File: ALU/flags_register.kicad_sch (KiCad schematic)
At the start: 7 parts, among them U6 SN74F86N, U8 Dual D FF

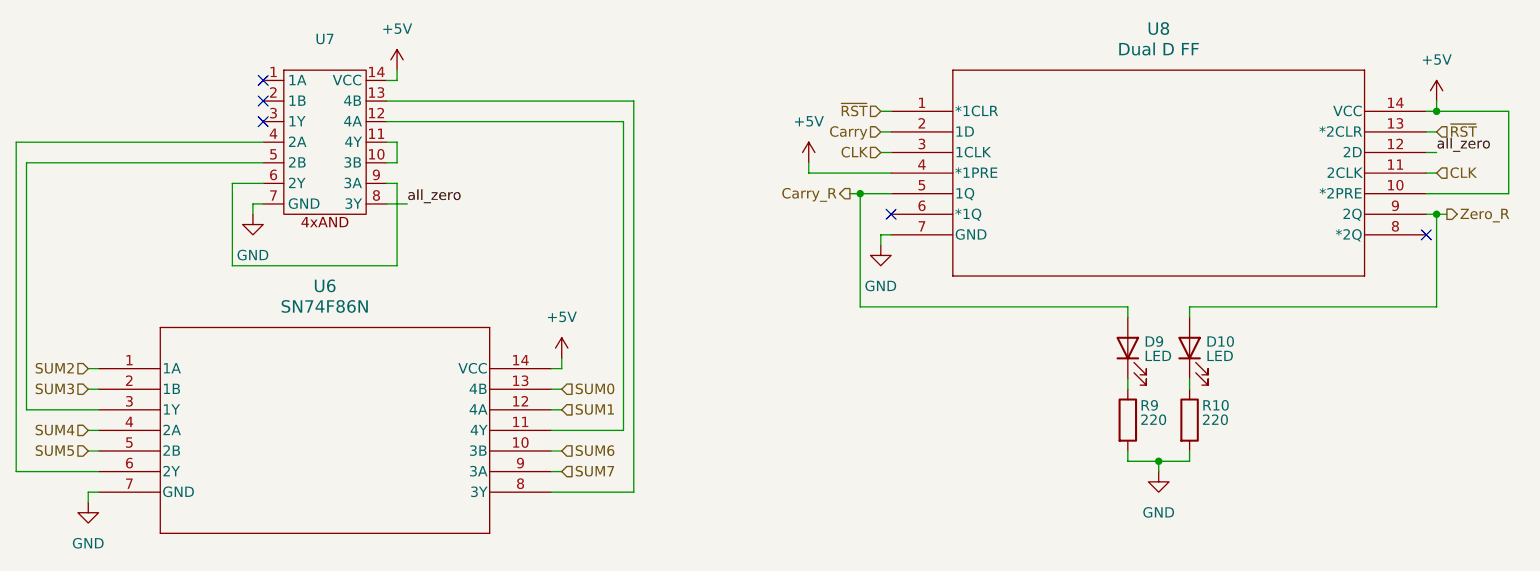
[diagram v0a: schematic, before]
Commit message: 4x NOR pinout was wrong. Updated with correct pinout. Fixed 2x D flip-flop references
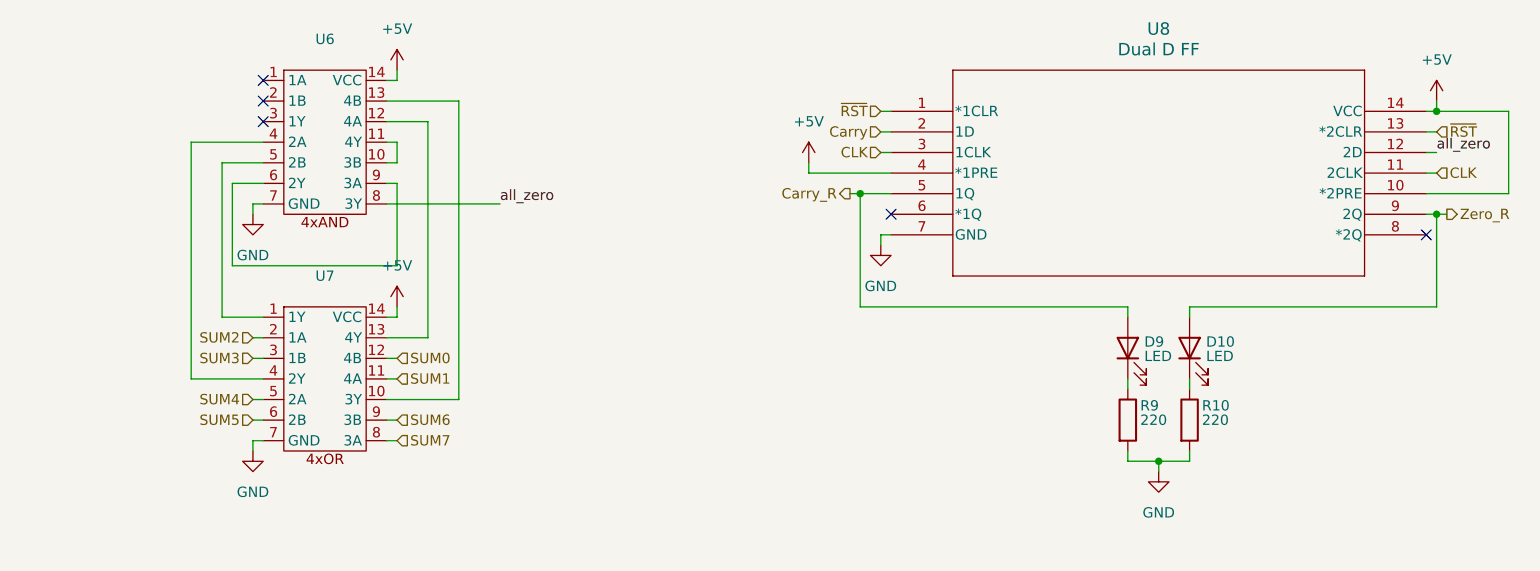
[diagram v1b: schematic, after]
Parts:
- removed U6: SN74F86N, _DownloadFootprints:4x_nor, symbol 4x_xor:SN74F86N
- added U7: ~, Package_DIP:DIP-14_W7.62mm, symbol 8BitCPU:4x_or
- U8: symbol 4x_D_FF:SN74HC74N -> 2x_D_FF:SN74HC74N
- renumbered U7 to U6
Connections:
- net +5V: now also U7.14 (VCC)
- net GND: now also U7.7 (GND)
- net SUM0: now also U7.12 (4B)
- net SUM1: now also U7.11 (4A)
- net SUM2: now also U7.2 (1A)
- net SUM3: now also U7.3 (1B)
- net SUM4: now also U7.5 (2A)
- net SUM5: now also U7.6 (2B)
- net SUM6: now also U7.9 (3B)
- net SUM7: now also U7.8 (3A)
- net at U6.12 (4A): now also U7.13 (4Y)
- net at U6.5 (2B): now also U7.1 (1Y)
- net at U6.4 (2A): now also U7.4 (2Y)
- net at U6.13 (4B): now also U7.10 (3Y)

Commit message: Fixed NOR schematic labeled as OR in ALU
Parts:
- removed U7: ~, Package_DIP:DIP-14_W7.62mm, symbol 8BitCPU:4x_or
- added U7: ~, Package_DIP:DIP-14_W7.62mm, symbol 8BitCPU:4x_nor
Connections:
- net +5V: now also U7.14 (VCC)
- net GND: now also U7.7 (GND)
- net SUM0: now also U7.12 (4B)
- net SUM1: now also U7.11 (4A)
- net SUM2: now also U7.2 (1A)
- net SUM3: now also U7.3 (1B)
- net SUM4: now also U7.5 (2A)
- net SUM5: now also U7.6 (2B)
- net SUM6: now also U7.9 (3B)
- net SUM7: now also U7.8 (3A)
- net at U6.5 (2B): now also U7.1 (1Y)
- net at U6.13 (4B): now also U7.10 (3Y)
- net at U6.12 (4A): now also U7.13 (4Y)
- net at U6.4 (2A): now also U7.4 (2Y)
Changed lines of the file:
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@@
-	)
-	(symbol
-		(lib_id "8BitCPU:4x_or")
-		(at 99.06 107.95 0)
-		(unit 1)
-		(exclude_from_sim no)
-		(in_bom yes)
-		(on_board yes)
-		(dnp no)
-		(fields_autoplaced yes)
-		(property "Reference" "U7"
-			(at 99.06 96.52 0)
-			(effects
-				(font
-					(size 1.27 1.27)
-				)
-			)
-		)
-		(property "Value" "~"
-			(at 99.06 99.06 0)
-			(effects
-				(font
-					(size 1.27 1.27)
-				)
-			)
-		)
-		(property "Footprint" "Package_DIP:DIP-14_W7.62mm"
-			(at 99.06 107.95 0)
-			(effects
-				(font
-					(size 1.27 1.27)
-				)
-				(hide yes)
-			)
-		)
-		(property "Datasheet" ""
-			(at 99.06 107.95 0)
-			(effects
-				(font
-					(size 1.27 1.27)
-				)
-				(hide yes)
-			)
-		)
-		(property "Description" ""
-			(at 99.06 107.95 0)
-			(effects
-				(font
-					(size 1.27 1.27)
-				)
-				(hide yes)
-			)
-		)
-		(pin "5"
-		)
-		(pin "7"
-		)
-		(pin "12"
-		)
-		(pin "13"
-		)
-		(pin "9"
-		)
-		(pin "4"
-		)
-		(pin "6"
-		)
-		(pin "10"
-		)
-		(pin "14"
-		)
-		(pin "2"
-		)
-		(pin "3"
-		)
-		(pin "8"
-		)
-		(pin "11"
-		)
-		(pin "1"
-		)
-		(instances
-			(project ""
-				(path "/62101b97-a334-4edf-8cb6-c85e816b5b90/6c41eb69-b663-40ea-b582-19e471384745"
-					(reference "U7")
-					(unit 1)
-				)
-			)
-		)
 	)
 	(symbol
@@
 					(unit 1)
 				)
+			)
+		)
+	)
+	(symbol
+		(lib_id "8BitCPU:4x_nor")
+		(at 99.06 107.95 0)
+		(unit 1)
+		(exclude_from_sim no)
+		(in_bom yes)
+		(on_board yes)
+		(dnp no)
+		(fields_autoplaced yes)
+		(property "Reference" "U7"
+			(at 99.06 96.52 0)
+			(effects
+				(font
+					(size 1.27 1.27)
+				)
+			)
+		)
+		(property "Value" "~"
+			(at 99.06 99.06 0)
+			(effects
+				(font
+					(size 1.27 1.27)
+				)
+			)
+		)
+		(property "Footprint" "Package_DIP:DIP-14_W7.62mm"
+			(at 99.06 107.95 0)
+			(effects
+				(font
+					(size 1.27 1.27)
+				)
+				(hide yes)
+			)
+		)
+		(property "Datasheet" ""
+			(at 99.06 107.95 0)
+			(effects
+				(font
+					(size 1.27 1.27)
+				)
+				(hide yes)
+			)
+		)
+		(property "Description" ""
+			(at 99.06 107.95 0)
+			(effects
+				(font
+					(size 1.27 1.27)
+				)
+				(hide yes)
+			)
+		)
+		(pin "6"
+		)
+		(pin "1"
+		)
+		(pin "13"
+		)
+		(pin "11"
+		)
+		(pin "2"
+		)
+		(pin "3"
+		)
+		(pin "8"
+		)
+		(pin "7"
+		)
+		(pin "5"
+		)
+		(pin "14"
+		)
+		(pin "12"
+		)
+		(pin "9"
+		)
+		(pin "10"
+		)
+		(pin "4"
+		)
+		(instances
+			(project ""
+				(path "/62101b97-a334-4edf-8cb6-c85e816b5b90/6c41eb69-b663-40ea-b582-19e471384745"
+					(reference "U7")
+					(unit 1)
+				)

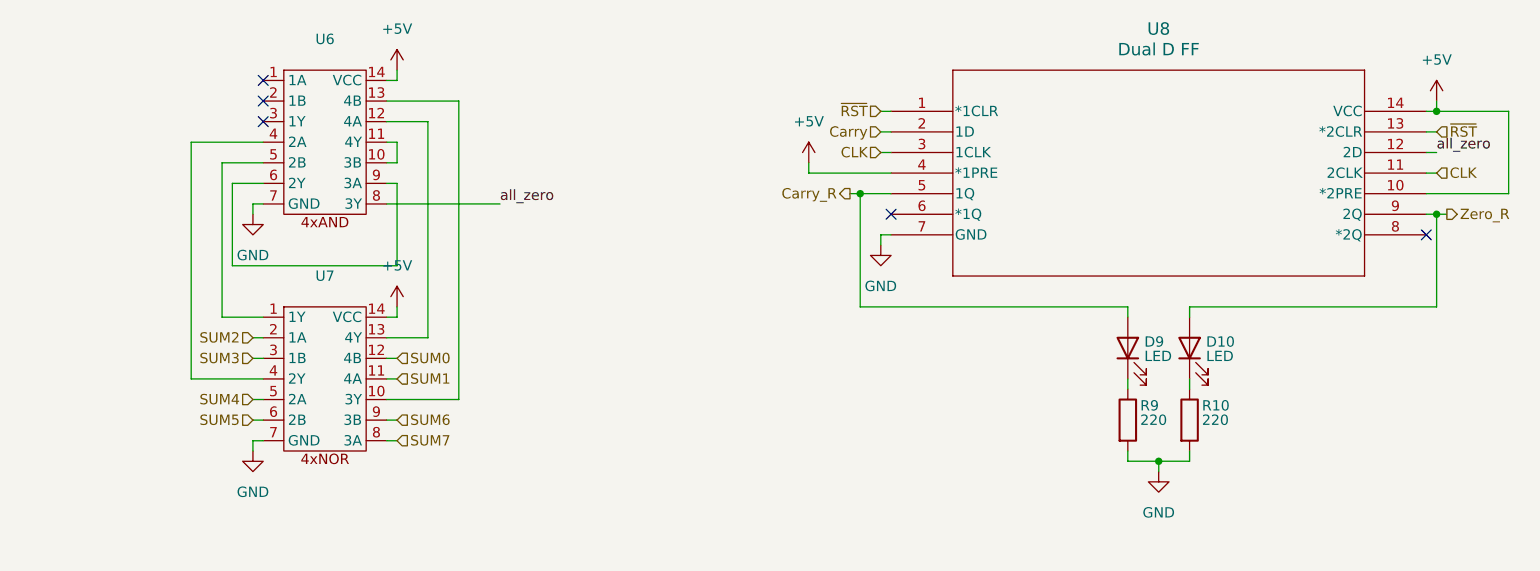
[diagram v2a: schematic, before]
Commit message: Forgot Flags register input enable. Passing clock though spare AND gate with new input Flag In input to create equvilant
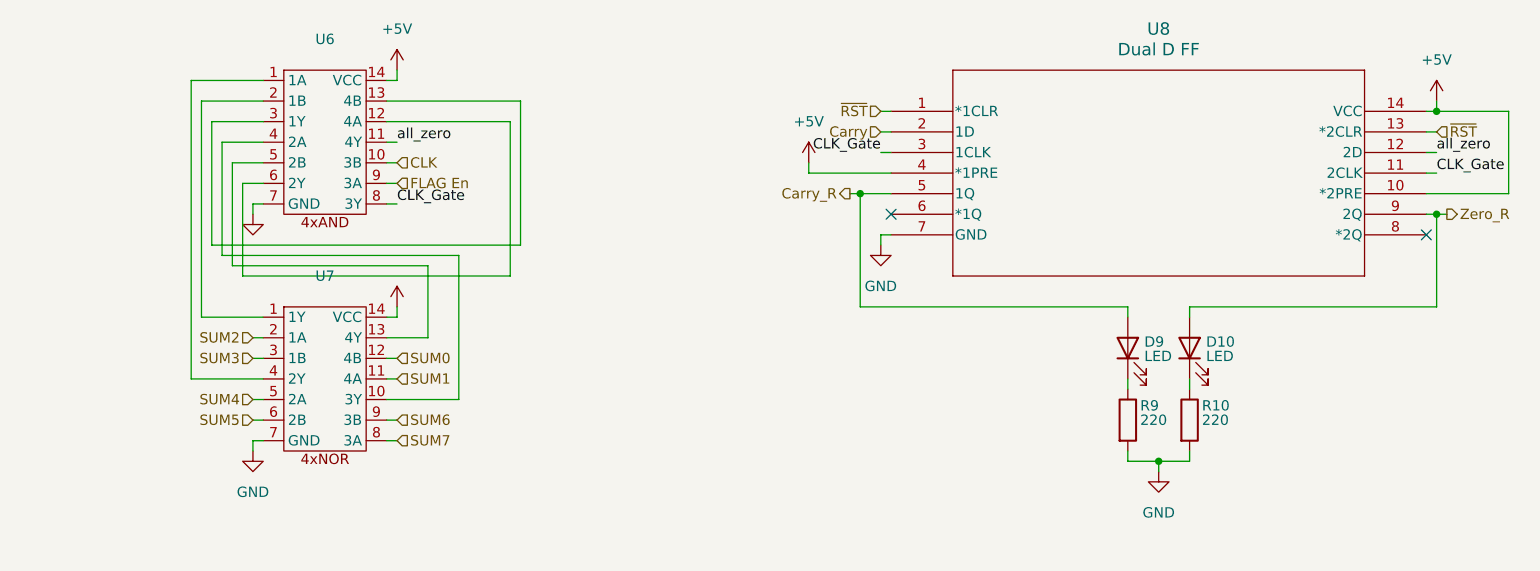
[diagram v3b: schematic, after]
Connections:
- net CLK: now also U6.10 (3B); no longer U8.11 (2CLK), U8.3 (1CLK)
- net all_zero: now also U6.11 (4Y); no longer U6.8 (3Y)
- net at U7.1 (1Y): now also U6.2 (1B); no longer U6.5 (2B)
- net at U7.10 (3Y): now also U6.4 (2A); no longer U6.13 (4B)
- net at U7.13 (4Y): now also U6.5 (2B); no longer U6.12 (4A)
- net at U7.4 (2Y): now also U6.1 (1A); no longer U6.4 (2A)
- net at U6.3 (1Y): now also U6.13 (4B)
- net at U6.6 (2Y): now also U6.12 (4A); no longer U6.9 (3A)
- new net CLK_Gate: U6.8 (3Y), U8.11 (2CLK), U8.3 (1CLK)
- new net FLAG En: U6.9 (3A)
- no-connect marks 5 -> 2
